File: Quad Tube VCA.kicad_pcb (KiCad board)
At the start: 2 copper layers, 162.6 x 100.3 mm, 212 parts, among them IC1 TL072, IC2 LM358, IC3 TL072, IC4 LM358, IC5 TL072, IC6 LM358, IC7 TL072, IC8 LM358

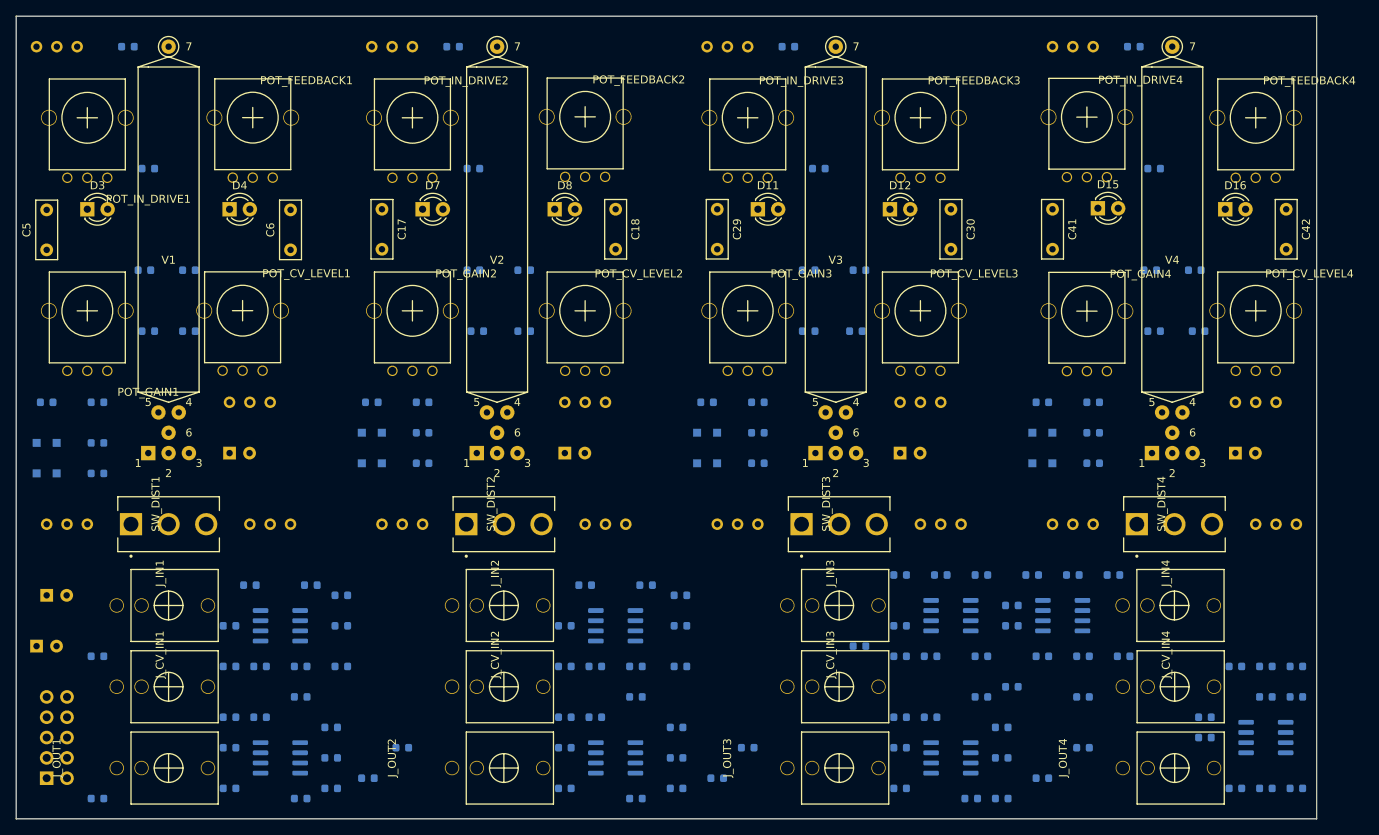
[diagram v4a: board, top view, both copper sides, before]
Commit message: starts work on power traces
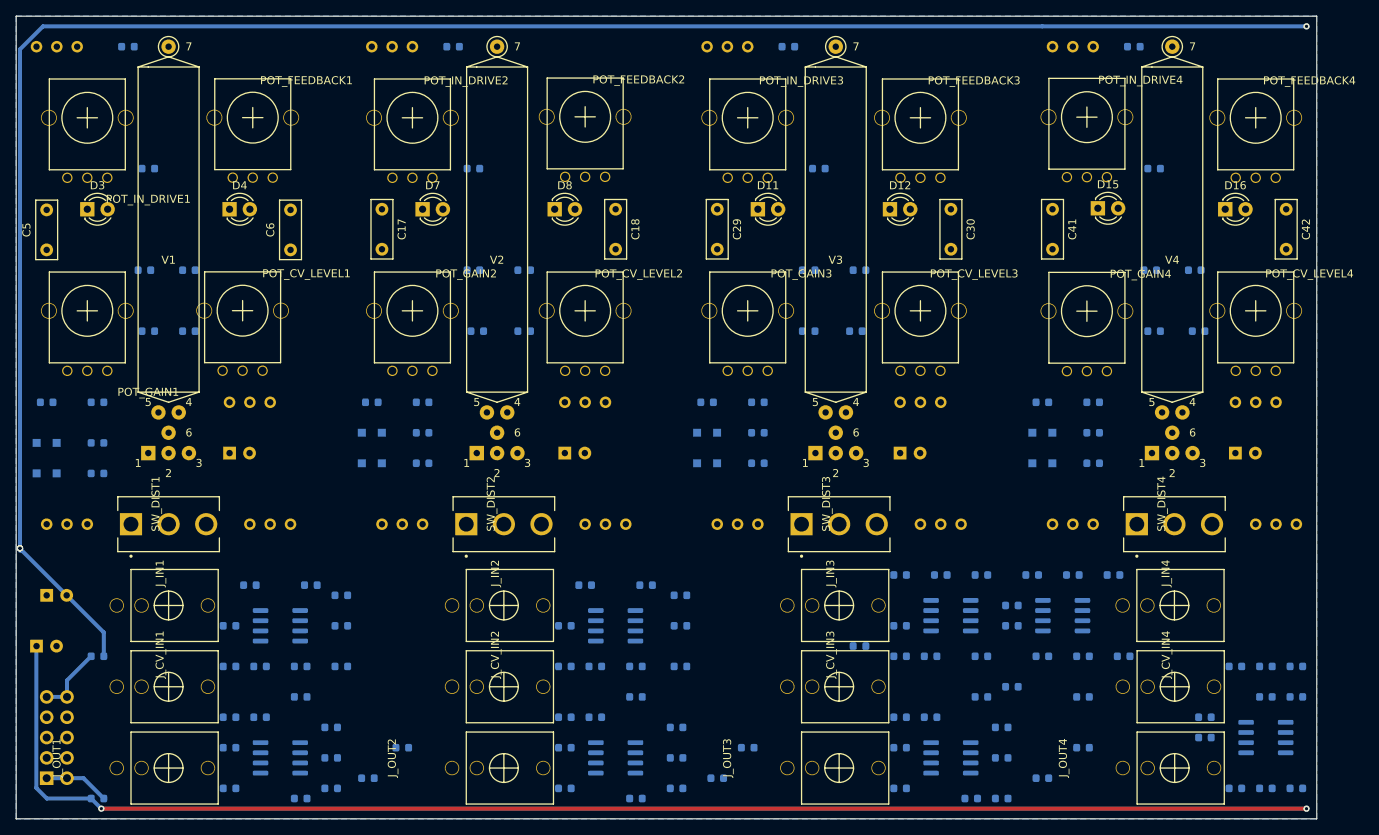
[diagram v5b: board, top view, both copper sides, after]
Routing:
- net +12V: track 0.00 -> 328.2 mm, vias 0 -> 2
- net -12V: track 0.00 -> 242.5 mm, vias 0 -> 3
- net Net-(FB2-Pad1): track 0.00 -> 8.87 mm
- net Net-(FB1-Pad1): track 0.00 -> 8.19 mm
- added copper zone on B.Cu, net GND
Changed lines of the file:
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@@
     (thickness 1.6)
     (drawings 4)
-    (tracks 0)
+    (tracks 29)
     (zones 0)
     (modules 212)
@@
   )
   (setup
-    (last_trace_width 0.25)
+    (last_trace_width 0.5)
     (user_trace_width 0.5)
     (trace_clearance 0.2)
@@
   (gr_line (start 228.6 44.45) (end 66.04 44.45) (layer Edge.Cuts) (width 0.05))
   (gr_line (start 228.6 144.78) (end 228.6 44.45) (layer Edge.Cuts) (width 0.05))
+  (segment (start 68.549999 140.910001) (end 69.879998 142.24) (width 0.5) (layer B.Cu) (net 4))
+  (segment (start 69.879998 142.24) (end 75.4125 142.24) (width 0.5) (layer B.Cu) (net 4))
+  (segment (start 68.549999 123.220001) (end 68.549999 140.910001) (width 0.5) (layer B.Cu) (net 4))
+  (segment (start 68.58 123.19) (end 68.549999 123.220001) (width 0.5) (layer B.Cu) (net 4))
+  (segment (start 76.6825 143.51) (end 227.33 143.51) (width 0.5) (layer B.Cu) (net 4))
+  (via (at 227.33 143.51) (size 0.8) (drill 0.4) (layers F.Cu B.Cu) (net 4))
+  (segment (start 75.4125 142.24) (end 76.6825 143.51) (width 0.5) (layer B.Cu) (net 4))
+  (via (at 76.6825 143.51) (size 0.8) (drill 0.4) (layers F.Cu B.Cu) (net 4))
+  (segment (start 227.33 143.51) (end 76.6825 143.51) (width 0.5) (layer F.Cu) (net 4))
+  (segment (start 76.9875 121.4775) (end 72.35 116.84) (width 0.5) (layer B.Cu) (net 5))
+  (segment (start 76.9875 124.46) (end 76.9875 121.4775) (width 0.5) (layer B.Cu) (net 5))
+  (via (at 227.33 45.72) (size 0.8) (drill 0.4) (layers F.Cu B.Cu) (net 5))
+  (segment (start 66.51501 111.00501) (end 66.51501 110.96501) (width 0.5) (layer B.Cu) (net 5))
+  (segment (start 72.35 116.84) (end 66.51501 111.00501) (width 0.5) (layer B.Cu) (net 5))
+  (segment (start 66.51501 111.28499) (end 66.51501 110.96501) (width 0.5) (layer B.Cu) (net 5))
+  (segment (start 66.51501 110.96501) (end 66.51501 110.96501) (width 0.5) (layer B.Cu) (net 5))
+  (via (at 66.51501 110.96501) (size 0.8) (drill 0.4) (layers F.Cu B.Cu) (net 5))
+  (segment (start 66.51501 110.96501) (end 66.51501 110.96501) (width 0.5) (layer B.Cu) (net 5))
+  (via (at 66.51501 110.96501) (size 0.8) (drill 0.4) (layers F.Cu B.Cu) (net 5))
+  (segment (start 194.31 45.72) (end 227.33 45.72) (width 0.5) (layer B.Cu) (net 5))
+  (segment (start 66.51501 48.593388) (end 69.388398 45.72) (width 0.5) (layer B.Cu) (net 5))
+  (segment (start 69.388398 45.72) (end 194.31 45.72) (width 0.5) (layer B.Cu) (net 5))
+  (segment (start 66.51501 110.96501) (end 66.51501 48.593388) (width 0.5) (layer B.Cu) (net 5))
+  (segment (start 69.85 139.7) (end 72.39 139.7) (width 0.5) (layer B.Cu) (net 127))
+  (segment (start 74.4475 139.7) (end 76.9875 142.24) (width 0.5) (layer B.Cu) (net 127))
+  (segment (start 72.39 139.7) (end 74.4475 139.7) (width 0.5) (layer B.Cu) (net 127))
+  (segment (start 69.85 129.54) (end 72.39 129.54) (width 0.5) (layer B.Cu) (net 128))
+  (segment (start 72.39 127.4825) (end 75.4125 124.46) (width 0.5) (layer B.Cu) (net 128))
+  (segment (start 72.39 129.54) (end 72.39 127.4825) (width 0.5) (layer B.Cu) (net 128))
+  (zone (net 3) (net_name GND) (layer B.Cu) (hatch edge 0.508)
+    (connect_pads (clearance 0.508))
+    (min_thickness 0.254)
+    (fill yes (arc_segments 32) (thermal_gap 0.508) (thermal_bridge_width 0.508))
+    (polygon
+      (pts
+        (xy 228.6 144.78) (xy 66.04 144.78) (xy 66.04 44.45) (xy 228.6 44.45)
+      )
+    )
+  )
 )

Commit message: routes power traces
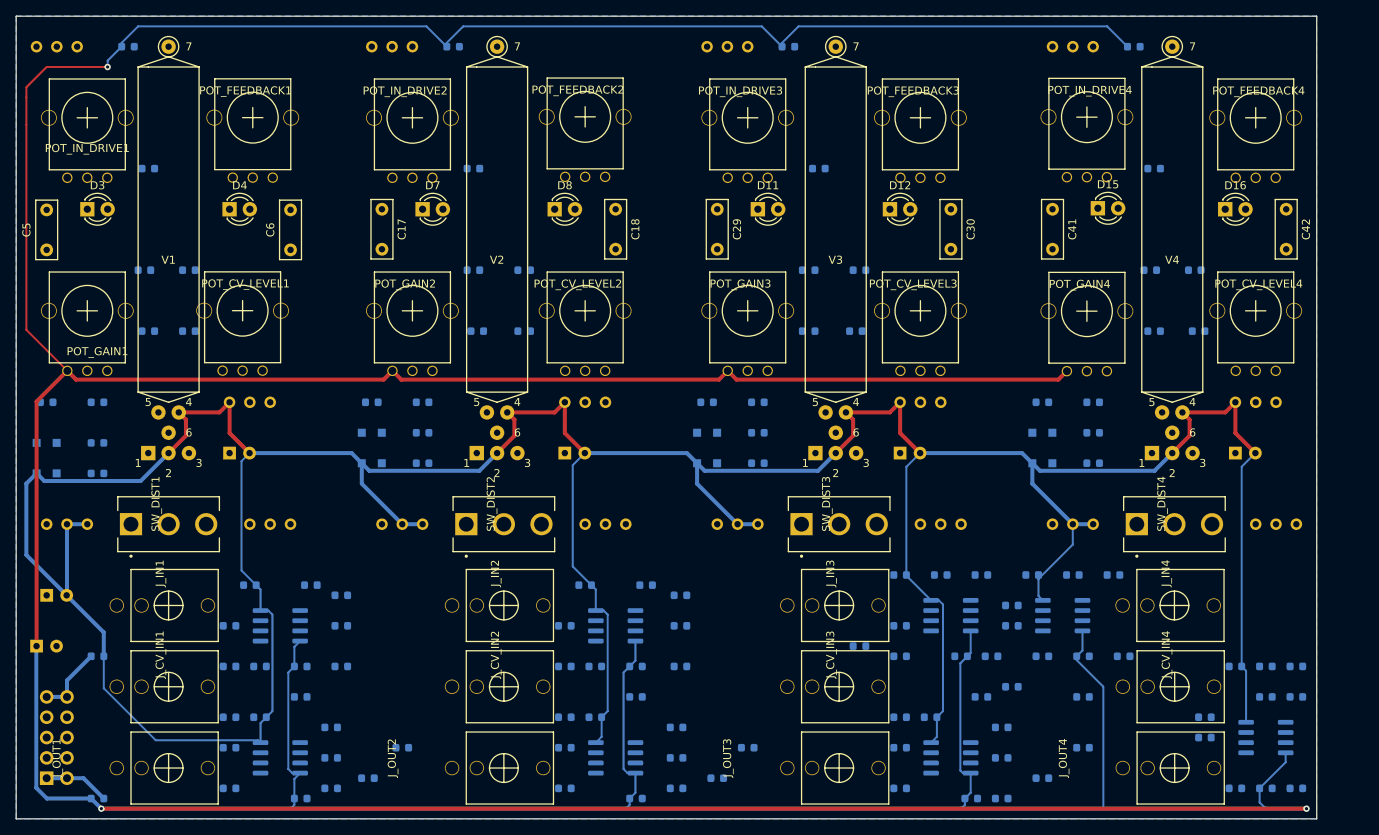
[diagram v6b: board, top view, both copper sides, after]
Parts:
- moved C35 3.81 mm to (184.2, 124.5)
- moved R55 1.27 mm to (188.0, 124.5)
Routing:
- net +12V: track 328.2 -> 780.3 mm, vias 2 -> 3
- net -12V: track 242.5 -> 469.5 mm, vias 3 -> 0

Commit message: routes nets for vca4 op amps
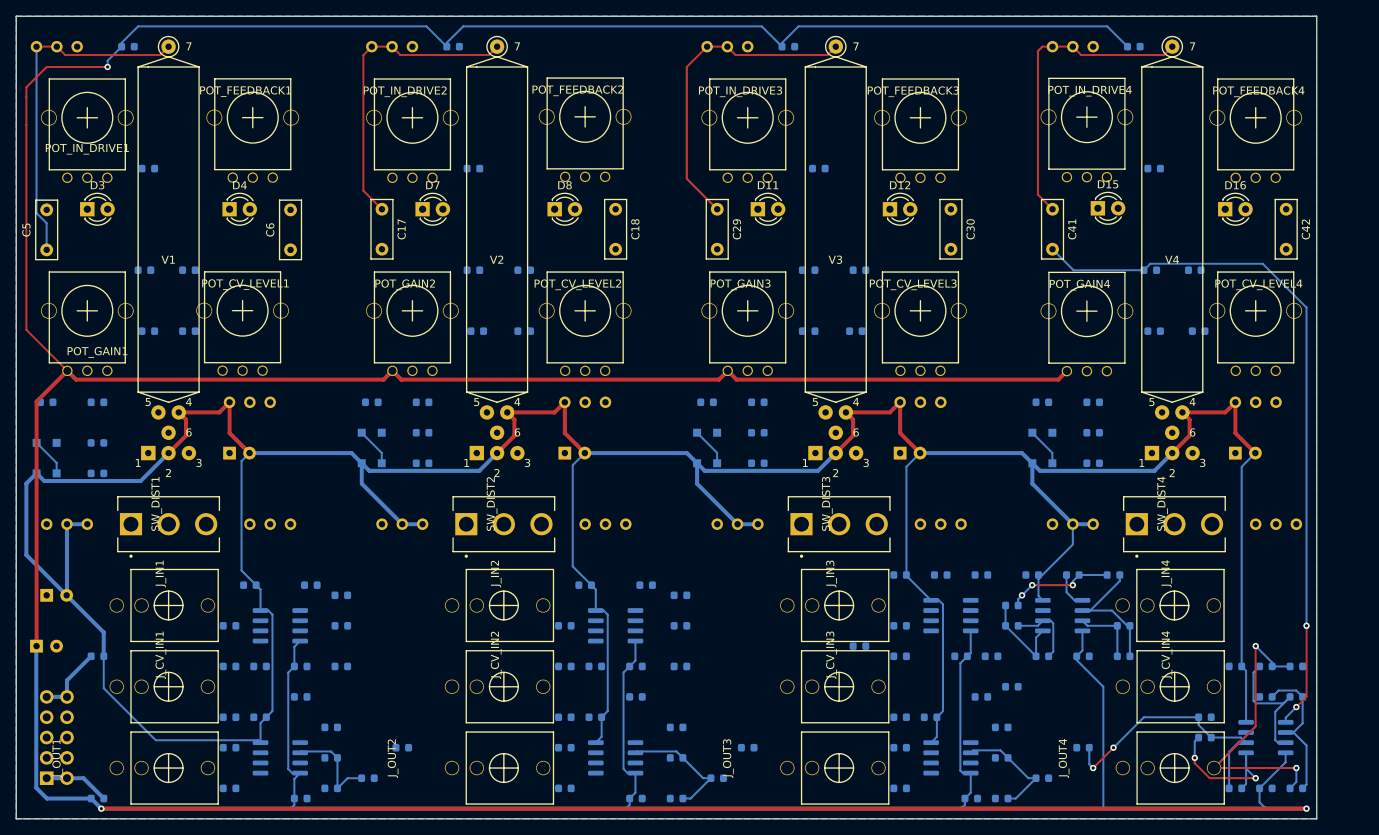
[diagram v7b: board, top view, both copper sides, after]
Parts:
- moved C44 10.2 mm to (204.5, 120.7), turned to 180 degrees
- moved R23 1.27 mm to (148.6, 142.2), turned to 180 degrees
- turned C40 to 180 degrees
- turned C45 to 180 degrees
- turned C50 to 180 degrees
- turned R64 to 180 degrees
- turned R75 to 180 degrees
- turned R76 to 180 degrees
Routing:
- net Net-(C41-Pad2): track 0.00 -> 88.4 mm, vias 0 -> 2
- net Net-(C5-Pad1): track 0.00 -> 43.3 mm
- net Net-(C29-Pad1): track 0.00 -> 39.9 mm
- net Net-(C41-Pad1): track 0.00 -> 38.4 mm
- net Net-(C17-Pad1): track 0.00 -> 38.2 mm
- net Net-(J_OUT4-Pad3): track 0.00 -> 36.2 mm, vias 0 -> 3
- net Net-(C39-Pad2): track 0.00 -> 33.5 mm, vias 0 -> 2
- net Net-(C39-Pad1): track 0.00 -> 20.2 mm, vias 0 -> 2
- net Net-(C40-Pad1): track 0.00 -> 18.2 mm
- net Net-(C44-Pad1): track 0.00 -> 17.5 mm
- net Net-(C40-Pad2): track 0.00 -> 17.2 mm
- net Net-(C16-Pad1): track 0.00 -> 15.4 mm
- net Net-(C28-Pad1): track 0.00 -> 14.3 mm
- net Net-(C50-Pad1): track 0.00 -> 13.4 mm, vias 0 -> 3
- net Net-(C4-Pad1): track 0.00 -> 12.4 mm
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
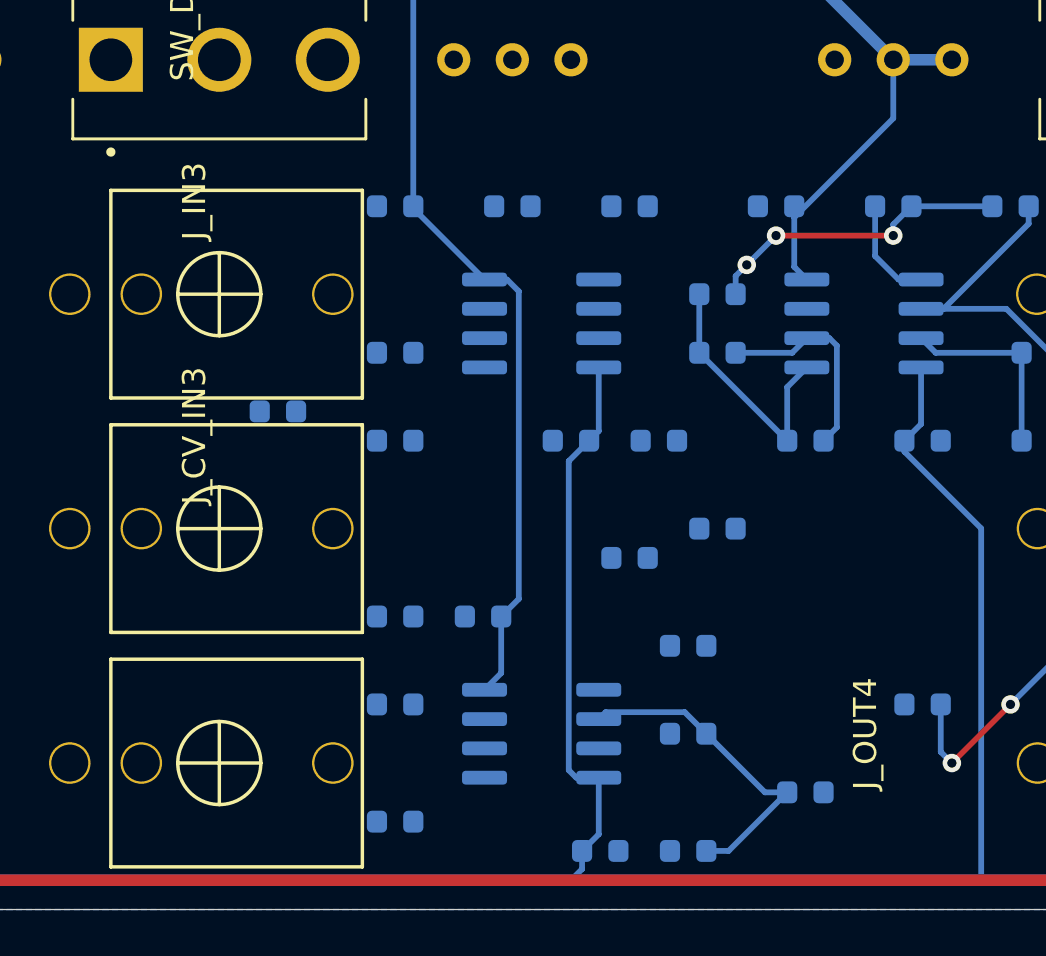
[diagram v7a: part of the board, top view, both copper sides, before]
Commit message: routes nets for remaining op amps
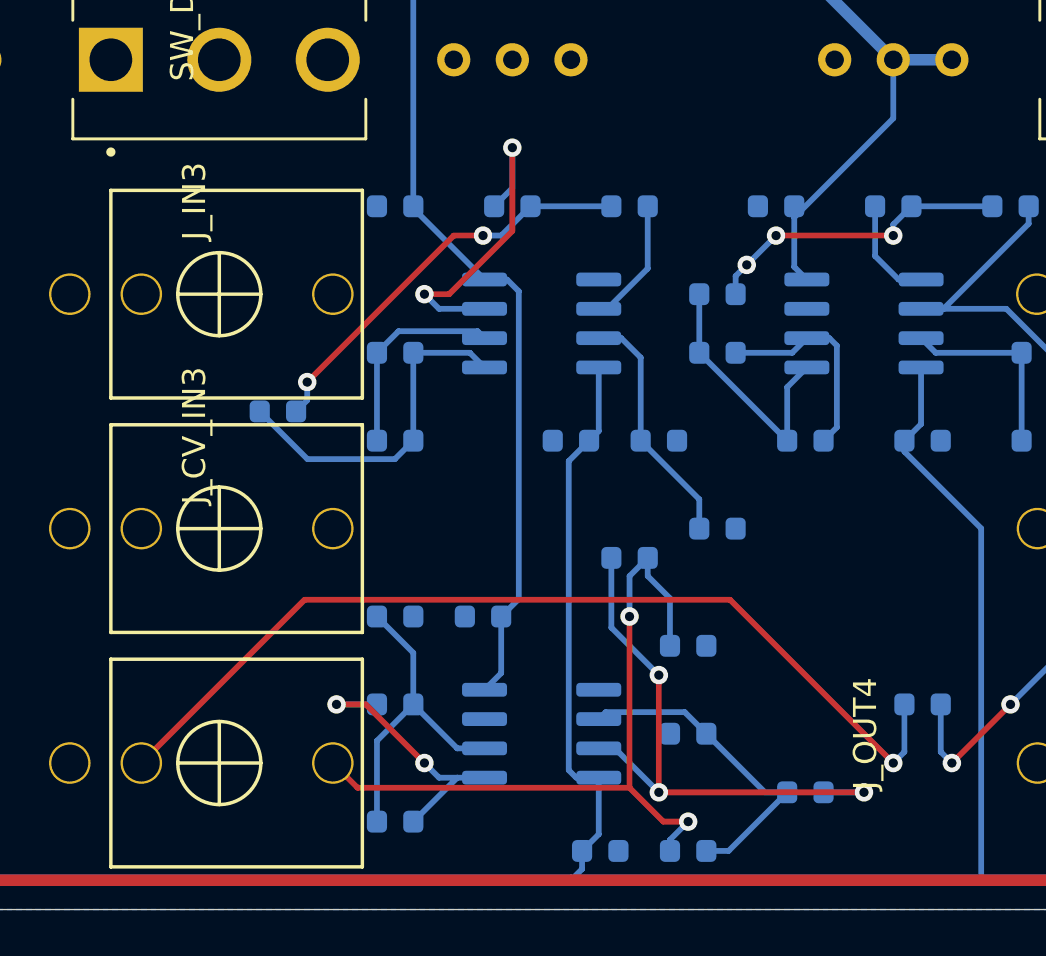
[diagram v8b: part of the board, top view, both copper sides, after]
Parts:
- turned C32 to 180 degrees
- turned C38 to 180 degrees
- turned R44 to 180 degrees
- turned R55 to 180 degrees
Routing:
- net Net-(J_OUT3-Pad2): track 0.00 -> 41.2 mm, vias 0 -> 1
- net Net-(J_OUT3-Pad3): track 0.00 -> 32.5 mm, vias 0 -> 2
- net Net-(C28-Pad2): track 0.00 -> 25.0 mm, vias 0 -> 3
- net Net-(C38-Pad1): track 0.00 -> 17.8 mm, vias 0 -> 2
- net Net-(C33-Pad2): track 0.00 -> 15.0 mm
- net GND: track 4.57 -> 18.9 mm, vias 0 -> 2
- net Net-(C27-Pad2): track 0.00 -> 14.1 mm
- net Net-(C27-Pad1): track 0.00 -> 12.2 mm, vias 0 -> 2
- net Net-(C32-Pad2): track 0.00 -> 10.6 mm
- net Net-(C33-Pad1): track 0.00 -> 8.98 mm
- net Net-(C32-Pad1): track 0.00 -> 5.54 mm
